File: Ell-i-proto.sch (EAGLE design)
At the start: 139 parts, among them J1 FTDI-SER-6, J10 PJ-102AX, J11 48V, J2 PWMH, J3 PWR, J4 PWML, J5 ANAL, J6 SPI, J7 COMM, J8 ANAH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

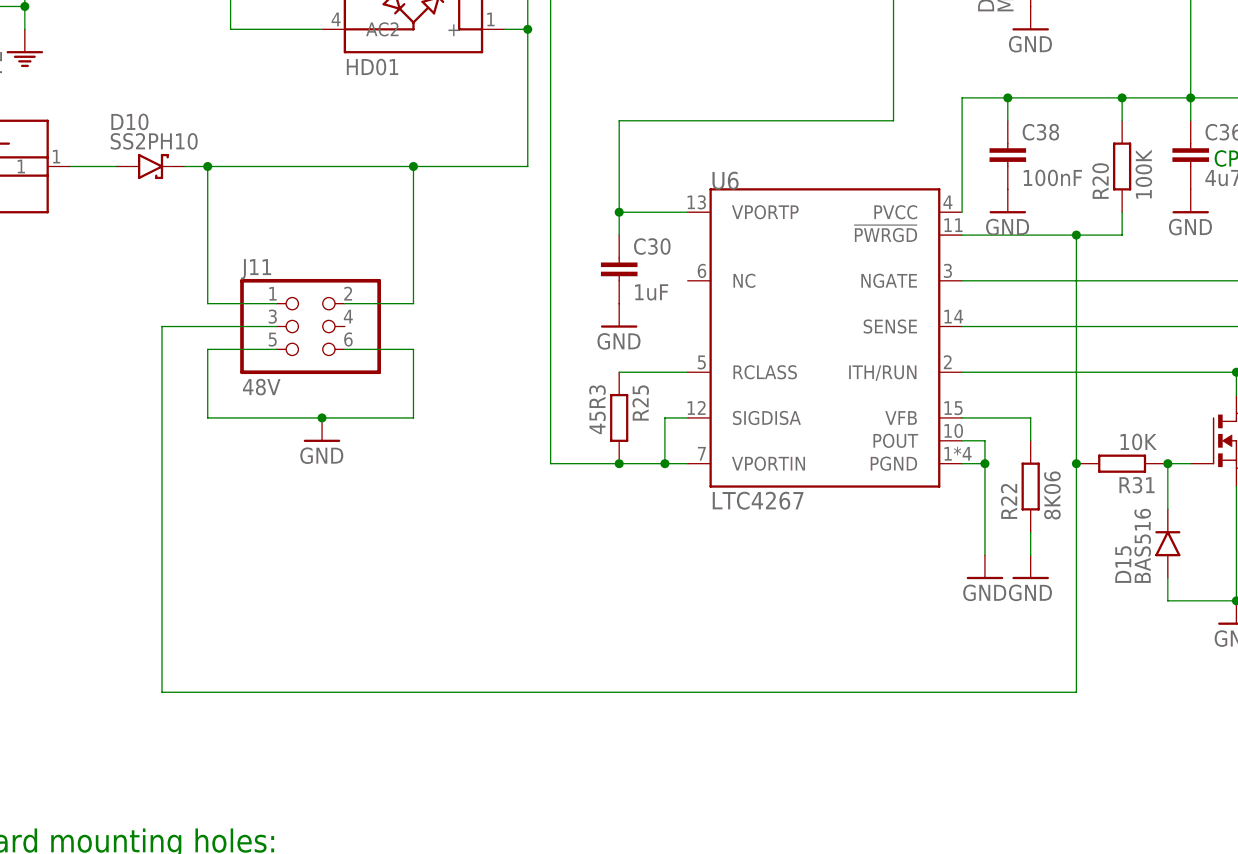
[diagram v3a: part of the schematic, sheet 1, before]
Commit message: rearrangement, T2 no more on the edge. Switch in 'location B', LEDs on the corner, etc
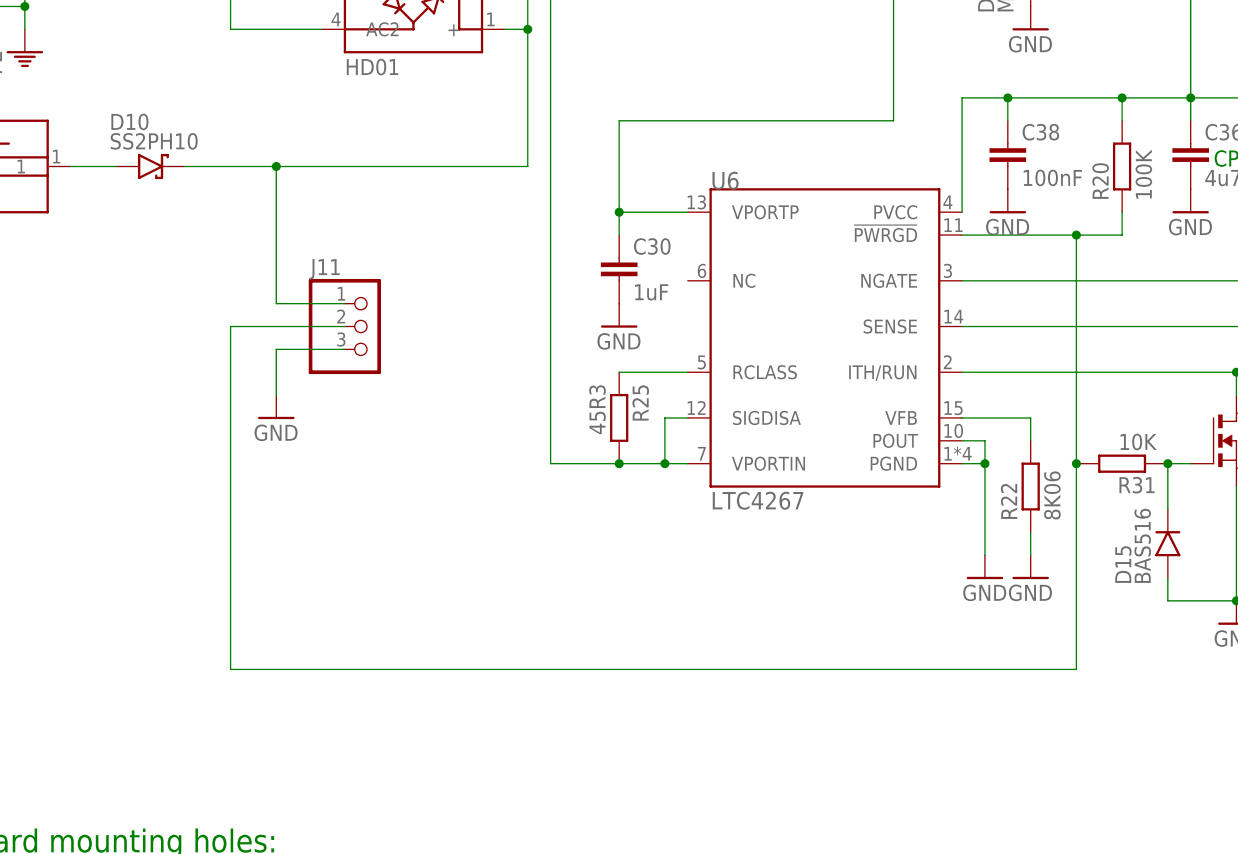
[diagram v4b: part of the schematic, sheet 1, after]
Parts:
- J11: value 48V -> (none); device ell-i:PINHD-2X3 -> pinhead:PINHD-1X3
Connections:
- net GND: now also J11.3; no longer J11.5, J11.6
- net NPWRGD: now also J11.2; no longer J11.3
- net V+: no longer J11.2
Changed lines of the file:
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@@
 <part name="J8" library="ell-i" deviceset="PINHD-1X8" device="" value="ANAH"/>
 <part name="J9" library="ell-i" deviceset="43860-0001" device="" value="RJ45"/>
-<part name="J11" library="ell-i" deviceset="PINHD-2X3" device="" value="48V"/>
 <part name="Q3" library="ell-i" deviceset="SI4848DY" device="" value="Si4848DY"/>
 <part name="Q4" library="ell-i" deviceset="FDV301N" device=""/>
@@
 <part name="H6" library="holes" deviceset="MOUNT-HOLE" device="3.2"/>
 <part name="S1" library="ell-i" deviceset="B3SL-10X2P" device=""/>
+<part name="J11" library="pinhead" deviceset="PINHD-1X3" device=""/>
 </parts>
 <sheets>
@@
 <instance part="D15" gate="G$1" x="149.86" y="68.58" rot="R90"/>
 <instance part="ISO1" gate="G$1" x="175.26" y="58.42" rot="R180"/>
-<instance part="J11" gate="G$1" x="53.34" y="91.44"/>
 <instance part="Q3" gate="G$1" x="193.04" y="99.06"/>
 <instance part="Q4" gate="G$1" x="157.48" y="78.74"/>
@@
 <instance part="GND21" gate="1" x="134.62" y="63.5"/>
 <instance part="GND22" gate="1" x="157.48" y="58.42"/>
-<instance part="GND23" gate="1" x="55.88" y="78.74"/>
+<instance part="GND23" gate="1" x="50.8" y="81.28"/>
 <instance part="GND24" gate="1" x="7.62" y="93.98"/>
 <instance part="GNDI4" gate="G$1" x="198.12" y="25.4"/>
@@
 <instance part="H5" gate="G$1" x="71.12" y="27.94"/>
 <instance part="H6" gate="G$1" x="71.12" y="12.7"/>
+<instance part="J11" gate="A" x="60.96" y="91.44"/>
 </instances>
 <busses>
@@
 </segment>
 <segment>
-<pinref part="J11" gate="G$1" pin="6"/>
-<pinref part="J11" gate="G$1" pin="5"/>
 <pinref part="GND23" gate="1" pin="GND"/>
-<wire x1="58.42" y1="88.9" x2="66.04" y2="88.9" width="0.1524" layer="91"/>
-<wire x1="66.04" y1="88.9" x2="66.04" y2="81.28" width="0.1524" layer="91"/>
-<wire x1="66.04" y1="81.28" x2="55.88" y2="81.28" width="0.1524" layer="91"/>
-<wire x1="55.88" y1="81.28" x2="43.18" y2="81.28" width="0.1524" layer="91"/>
-<wire x1="43.18" y1="81.28" x2="43.18" y2="88.9" width="0.1524" layer="91"/>
-<wire x1="43.18" y1="88.9" x2="50.8" y2="88.9" width="0.1524" layer="91"/>
-<junction x="55.88" y="81.28"/>
+<wire x1="50.8" y1="88.9" x2="50.8" y2="83.82" width="0.1524" layer="91"/>
+<pinref part="J11" gate="A" pin="3"/>
+<wire x1="50.8" y1="88.9" x2="58.42" y2="88.9" width="0.1524" layer="91"/>
 </segment>
 <segment>
@@
 <wire x1="78.74" y1="124.46" x2="78.74" y2="109.22" width="0.1524" layer="91"/>
 <junction x="78.74" y="124.46"/>
-<pinref part="J11" gate="G$1" pin="2"/>
-<wire x1="66.04" y1="93.98" x2="58.42" y2="93.98" width="0.1524" layer="91"/>
-<wire x1="78.74" y1="109.22" x2="66.04" y2="109.22" width="0.1524" layer="91"/>
-<wire x1="66.04" y1="109.22" x2="66.04" y2="93.98" width="0.1524" layer="91"/>
-<junction x="66.04" y="109.22"/>
-<wire x1="43.18" y1="109.22" x2="66.04" y2="109.22" width="0.1524" layer="91"/>
-<junction x="43.18" y="109.22"/>
-<wire x1="43.18" y1="93.98" x2="43.18" y2="109.22" width="0.1524" layer="91"/>
-<pinref part="J11" gate="G$1" pin="1"/>
-<wire x1="50.8" y1="93.98" x2="43.18" y2="93.98" width="0.1524" layer="91"/>
+<wire x1="78.74" y1="109.22" x2="50.8" y2="109.22" width="0.1524" layer="91"/>
+<wire x1="50.8" y1="109.22" x2="50.8" y2="93.98" width="0.1524" layer="91"/>
+<junction x="50.8" y="109.22"/>
+<wire x1="40.64" y1="109.22" x2="50.8" y2="109.22" width="0.1524" layer="91"/>
 <wire x1="78.74" y1="124.46" x2="78.74" y2="147.32" width="0.1524" layer="91"/>
 <junction x="78.74" y="147.32"/>
@@
 <wire x1="99.06" y1="149.86" x2="99.06" y2="147.32" width="0.1524" layer="91"/>
 <pinref part="D10" gate="G$1" pin="C"/>
-<wire x1="40.64" y1="109.22" x2="43.18" y2="109.22" width="0.1524" layer="91"/>
+<pinref part="J11" gate="A" pin="1"/>
+<wire x1="58.42" y1="93.98" x2="50.8" y2="93.98" width="0.1524" layer="91"/>
 </segment>
 </net>
@@
 <net name="NPWRGD" class="0">
 <segment>
-<pinref part="J11" gate="G$1" pin="3"/>
 <pinref part="R31" gate="G$1" pin="2"/>
-<wire x1="50.8" y1="91.44" x2="38.1" y2="91.44" width="0.1524" layer="91"/>
-<wire x1="38.1" y1="91.44" x2="38.1" y2="50.8" width="0.1524" layer="91"/>
-<wire x1="38.1" y1="50.8" x2="139.7" y2="50.8" width="0.1524" layer="91"/>
+<wire x1="45.72" y1="91.44" x2="45.72" y2="53.34" width="0.1524" layer="91"/>
+<wire x1="45.72" y1="53.34" x2="139.7" y2="53.34" width="0.1524" layer="91"/>
 <pinref part="U6" gate="G$1" pin="!PWRGD"/>
-<wire x1="139.7" y1="76.2" x2="139.7" y2="50.8" width="0.1524" layer="91"/>
+<wire x1="139.7" y1="76.2" x2="139.7" y2="53.34" width="0.1524" layer="91"/>
 <pinref part="R20" gate="G$1" pin="1"/>
 <wire x1="139.7" y1="76.2" x2="139.7" y2="101.6" width="0.1524" layer="91"/>
@@
 <junction x="139.7" y="76.2"/>
 <junction x="139.7" y="101.6"/>
-</segment>
-</net>
+<pinref part="J11" gate="A" pin="2"/>
+<wire x1="45.72" y1="91.44" x2="58.42" y2="91.44" width="0.1524" layer="91"/>
+</segment>
+</net>
